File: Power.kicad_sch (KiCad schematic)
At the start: 25 parts, among them J4 XT30, J5 Molex 470531000, Q1 DMP3013SFV-7, U4 EMC2301-1-ACZL-TR, U5 LMR33640DDDAR

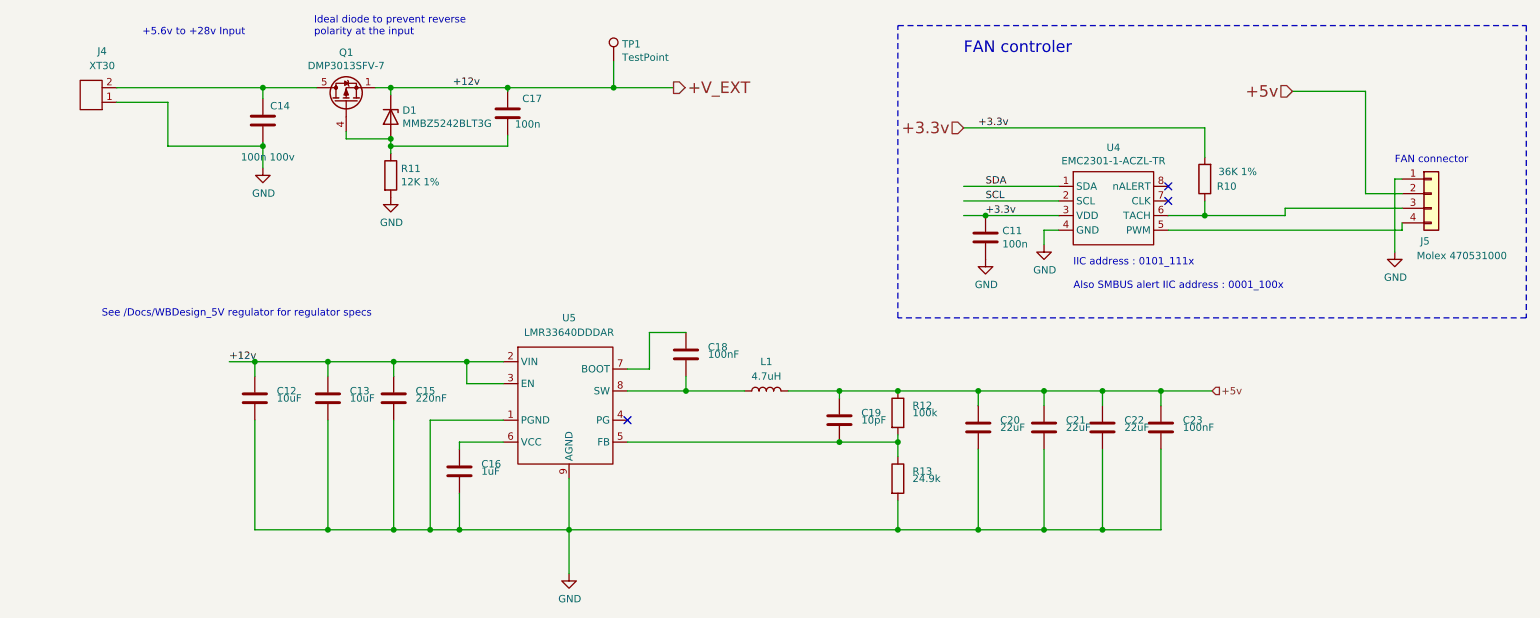
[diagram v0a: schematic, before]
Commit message: additional layout, power circuitry
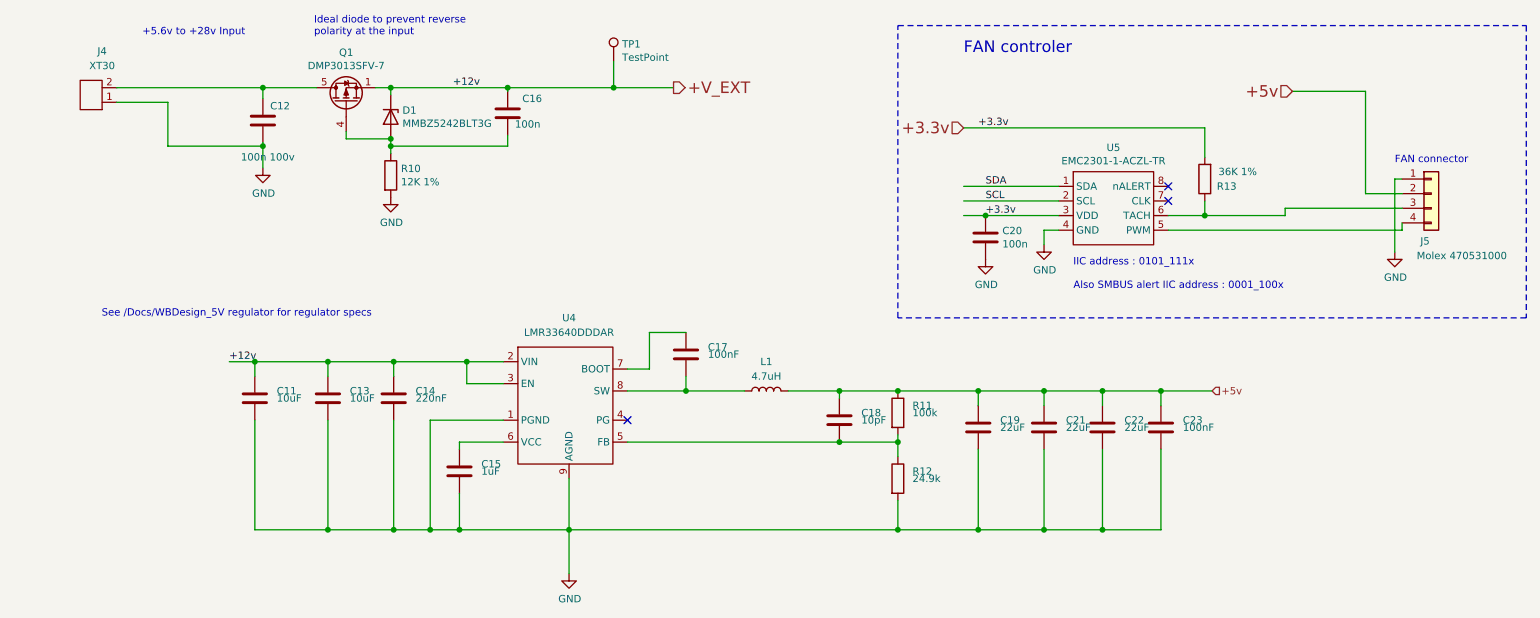
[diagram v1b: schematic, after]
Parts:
- L1: footprint Open-HD:IND_XAL6060-472MEB -> CM4IO:HCM1A1105V2-4R7-R
- renumbered C12 to C11, C14 to C12, C15 to C14, C16 to C15, C17 to C16, C18 to C17, C19 to C18, C20 to C19, C11 to C20, R11 to R10, R12 to R11, R13 to R12, R10 to R13, U5 to U4, U4 to U5
